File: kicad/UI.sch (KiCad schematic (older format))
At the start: 14 parts, among them SW2 SW_Push, U13 PCA9632, U14 LMV321

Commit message: 回路を改良
受光部をフォトトランジスタに変更
測距センサをVL6180Xに変更
動作電圧を3Vに変更
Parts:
- C21: renamed from C33; value 1u -> 10u
- SW2: footprint mouse:SW_PUSH -> mouse:SKRPACE010
- renumbered C32 to C20, D13 to D10, D10 to D7, D11 to D8, D12 to D9, R28 to R15, R29 to R16, R30 to R17, R31 to R18, U14 to U10, U13 to U9
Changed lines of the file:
@@
 LIBS:ftdi
 LIBS:gennum
-LIBS:graphic
 LIBS:hc11
 LIBS:ir
 LIBS:Lattice
 LIBS:leds
-LIBS:logo
 LIBS:maxim
 LIBS:mechanical
@@
 LIBS:zetex
 LIBS:Zilog
+LIBS:graphic_symbols
+LIBS:infineon
+LIBS:intersil
+LIBS:LEM
+LIBS:logic_programmable
+LIBS:RFSolutions
 LIBS:KERISE-cache
 EELAYER 25 0
@@
 $EndDescr
 $Comp
-L GND #PWR082
+L GND #PWR076
 U 1 1 57CEA2EF
 P 3700 6200
-F 0 "#PWR082" H 3700 5950 50  0001 C CNN
+F 0 "#PWR076" H 3700 5950 50  0001 C CNN
 F 1 "GND" H 3700 6050 50  0000 C CNN
 F 2 "" H 3700 6200 50  0000 C CNN
@@
 F 0 "SW2" H 3750 5900 50  0000 L CNN
 F 1 "SW_Push" H 3700 5740 50  0000 C CNN
-F 2 "mouse:SW_PUSH" H 3700 6000 50  0001 C CNN
+F 2 "mouse:SKRPACE010" H 3700 6000 50  0001 C CNN
 F 3 "" H 3700 6000 50  0001 C CNN
 	1    3700 5800
@@
 $EndComp
 $Comp
-L LMV321 U14
+L LMV321 U10
 U 1 1 5A1C2ABB
 P 5100 5800
-F 0 "U14" H 5100 6000 50  0000 L CNN
+F 0 "U10" H 5100 6000 50  0000 L CNN
 F 1 "LMV321" H 5100 5600 50  0000 L CNN
 F 2 "TO_SOT_Packages_SMD:SOT-353_SC-70-5" H 5100 5800 50  0001 L CNN
@@
 $EndComp
 $Comp
-L GND #PWR083
+L GND #PWR077
 U 1 1 5A1C53C4
 P 5800 6200
-F 0 "#PWR083" H 5800 5950 50  0001 C CNN
+F 0 "#PWR077" H 5800 5950 50  0001 C CNN
 F 1 "GND" H 5800 6050 50  0000 C CNN
 F 2 "" H 5800 6200 50  0000 C CNN
@@
 	5800 5900 5900 5900
 $Comp
-L C_Small C33
+L C_Small C21
 U 1 1 5A1C5465
 P 5700 5800
-F 0 "C33" H 5710 5870 50  0000 L CNN
-F 1 "1u" H 5710 5720 50  0000 L CNN
+F 0 "C21" H 5710 5870 50  0000 L CNN
+F 1 "10u" H 5710 5720 50  0000 L CNN
 F 2 "Capacitors_SMD:C_0402" H 5700 5800 50  0001 C CNN
 F 3 "" H 5700 5800 50  0001 C CNN
@@
 Connection ~ 5500 5800
 $Comp
-L +3.3V #PWR084
+L +3.3V #PWR078
 U 1 1 5A1C5659
 P 5000 5300
-F 0 "#PWR084" H 5000 5150 50  0001 C CNN
+F 0 "#PWR078" H 5000 5150 50  0001 C CNN
 F 1 "+3.3V" H 5000 5440 50  0000 C CNN
 F 2 "" H 5000 5300 50  0001 C CNN
@@
 	5000 5300 5000 5500
 $Comp
-L GND #PWR085
+L GND #PWR079
 U 1 1 5A1C56CE
 P 5000 6200
-F 0 "#PWR085" H 5000 5950 50  0001 C CNN
+F 0 "#PWR079" H 5000 5950 50  0001 C CNN
 F 1 "GND" H 5000 6050 50  0000 C CNN
 F 2 "" H 5000 6200 50  0000 C CNN
@@
 SDA
 $Comp
-L +3.3V #PWR086
+L +3.3V #PWR080
 U 1 1 5A202D5A
 P 4050 3150
-F 0 "#PWR086" H 4050 3000 50  0001 C CNN
+F 0 "#PWR080" H 4050 3000 50  0001 C CNN
 F 1 "+3.3V" H 4050 3290 50  0000 C CNN
 F 2 "" H 4050 3150 50  0001 C CNN
@@
 	4050 3150 4050 3650
 $Comp
-L GND #PWR087
+L GND #PWR081
 U 1 1 5A202F53
 P 4050 4650
-F 0 "#PWR087" H 4050 4400 50  0001 C CNN
+F 0 "#PWR081" H 4050 4400 50  0001 C CNN
 F 1 "GND" H 4050 4500 50  0000 C CNN
 F 2 "" H 4050 4650 50  0000 C CNN
@@
 	5050 3450 5050 3550
 $Comp
-L +3.3V #PWR088
+L +3.3V #PWR082
 U 1 1 5A204571
 P 5050 3150
-F 0 "#PWR088" H 5050 3000 50  0001 C CNN
+F 0 "#PWR082" H 5050 3000 50  0001 C CNN
 F 1 "+3.3V" H 5050 3290 50  0000 C CNN
 F 2 "" H 5050 3150 50  0001 C CNN
@@
 $EndComp
 $Comp
-L R R29
+L R R16
 U 1 1 5A20456B
 P 5050 3700
-F 0 "R29" V 5130 3700 50  0000 C CNN
+F 0 "R16" V 5130 3700 50  0000 C CNN
 F 1 "100" V 5050 3700 50  0000 C CNN
 F 2 "Resistors_SMD:R_0201" V 4980 3700 50  0001 C CNN
@@
 $EndComp
 $Comp
-L LED_Small D11
+L LED_Small D8
 U 1 1 5A204565
 P 5050 3350
-F 0 "D11" H 5000 3475 50  0000 L CNN
+F 0 "D8" H 5000 3475 50  0000 L CNN
 F 1 "LED" H 5000 3250 50  0000 L CNN
 F 2 "LEDs:LED_0402" V 5050 3350 50  0001 C CNN
@@
 	4750 3450 4750 3550
 $Comp
-L +3.3V #PWR089
+L +3.3V #PWR083
 U 1 1 5A203D72
 P 4750 3150
-F 0 "#PWR089" H 4750 3000 50  0001 C CNN
+F 0 "#PWR083" H 4750 3000 50  0001 C CNN
 F 1 "+3.3V" H 4750 3290 50  0000 C CNN
 F 2 "" H 4750 3150 50  0001 C CNN
@@
 $EndComp
 $Comp
-L R R28
+L R R15
 U 1 1 5A1FD2AD
 P 4750 3700
-F 0 "R28" V 4830 3700 50  0000 C CNN
+F 0 "R15" V 4830 3700 50  0000 C CNN
 F 1 "100" V 4750 3700 50  0000 C CNN
 F 2 "Resistors_SMD:R_0201" V 4680 3700 50  0001 C CNN
@@
 $EndComp
 $Comp
-L LED_Small D10
+L LED_Small D7
 U 1 1 5A203147
 P 4750 3350
-F 0 "D10" H 4700 3475 50  0000 L CNN
+F 0 "D7" H 4700 3475 50  0000 L CNN
 F 1 "LED" H 4700 3250 50  0000 L CNN
 F 2 "LEDs:LED_0402" V 4750 3350 50  0001 C CNN
@@
 	5650 3450 5650 3550
 $Comp
-L +3.3V #PWR090
+L +3.3V #PWR084
 U 1 1 5A20460C
 P 5650 3150
-F 0 "#PWR090" H 5650 3000 50  0001 C CNN
+F 0 "#PWR084" H 5650 3000 50  0001 C CNN
 F 1 "+3.3V" H 5650 3290 50  0000 C CNN
 F 2 "" H 5650 3150 50  0001 C CNN
@@
 $EndComp
 $Comp
-L R R31
+L R R18
 U 1 1 5A204612
 P 5650 3700
-F 0 "R31" V 5730 3700 50  0000 C CNN
+F 0 "R18" V 5730 3700 50  0000 C CNN
 F 1 "100" V 5650 3700 50  0000 C CNN
 F 2 "Resistors_SMD:R_0201" V 5580 3700 50  0001 C CNN
@@
 $EndComp
 $Comp
-L LED_Small D13
+L LED_Small D10
 U 1 1 5A204618
 P 5650 3350
-F 0 "D13" H 5600 3475 50  0000 L CNN
+F 0 "D10" H 5600 3475 50  0000 L CNN
 F 1 "LED" H 5600 3250 50  0000 L CNN
 F 2 "LEDs:LED_0402" V 5650 3350 50  0001 C CNN
@@
 	5350 3450 5350 3550
 $Comp
-L +3.3V #PWR091
+L +3.3V #PWR085
 U 1 1 5A204620
 P 5350 3150
-F 0 "#PWR091" H 5350 3000 50  0001 C CNN
+F 0 "#PWR085" H 5350 3000 50  0001 C CNN
 F 1 "+3.3V" H 5350 3290 50  0000 C CNN
 F 2 "" H 5350 3150 50  0001 C CNN
@@
 $EndComp
 $Comp
-L R R30
+L R R17
 U 1 1 5A204626
 P 5350 3700
-F 0 "R30" V 5430 3700 50  0000 C CNN
+F 0 "R17" V 5430 3700 50  0000 C CNN
 F 1 "100" V 5350 3700 50  0000 C CNN
 F 2 "Resistors_SMD:R_0201" V 5280 3700 50  0001 C CNN
@@
 $EndComp
 $Comp
-L LED_Small D12
+L LED_Small D9
 U 1 1 5A20462C
 P 5350 3350
-F 0 "D12" H 5300 3475 50  0000 L CNN
+F 0 "D9" H 5300 3475 50  0000 L CNN
 F 1 "LED" H 5300 3250 50  0000 L CNN
 F 2 "LEDs:LED_0402" V 5350 3350 50  0001 C CNN
@@
 	5650 4250 5650 3850
 $Comp
-L C_Small C32
+L C_Small C20
 U 1 1 5A2A1F42
 P 3850 3450
-F 0 "C32" H 3860 3520 50  0000 L CNN
+F 0 "C20" H 3860 3520 50  0000 L CNN
 F 1 "0.1u" H 3860 3370 50  0000 L CNN
 F 2 "Capacitors_SMD:C_0201" H 3850 3450 50  0001 C CNN
@@
 $EndComp
 $Comp
-L GND #PWR092
+L GND #PWR086
 U 1 1 5A2A2041
 P 3850 3550
-F 0 "#PWR092" H 3850 3300 50  0001 C CNN
+F 0 "#PWR086" H 3850 3300 50  0001 C CNN
 F 1 "GND" H 3850 3400 50  0000 C CNN
 F 2 "" H 3850 3550 50  0001 C CNN
@@
 Connection ~ 4050 3250
 $Comp
-L PCA9632 U13
+L PCA9632 U9
 U 1 1 5A2BFCCE
 P 4050 4100
-F 0 "U13" H 3550 4425 50  0000 L CNN
+F 0 "U9" H 3550 4425 50  0000 L CNN
 F 1 "PCA9632" H 4100 4425 50  0000 L CNN
 F 2 "mouse:DFN-8-1EP_3x3mm_Pitch0.5mm" H 4100 3800 50  0001 L CNN

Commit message: 部品を配置
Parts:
- removed C21: 10u, Capacitors_SMD:C_0402, symbol C_Small
- removed U10: LMV321, TO_SOT_Packages_SMD:SOT-353_SC-70-5, symbol LMV321
- added C19: 0.1u, Capacitors_SMD:C_0201_NoSilk, symbol C_Small
- C18: renamed from C20; footprint Capacitors_SMD:C_0201 -> Capacitors_SMD:C_0201_NoSilk
- R17: renamed from R15; footprint Resistors_SMD:R_0201 -> Resistors_SMD:R_0201_NoSilk
- R18: renamed from R16; footprint Resistors_SMD:R_0201 -> Resistors_SMD:R_0201_NoSilk
- R19: renamed from R17; footprint Resistors_SMD:R_0201 -> Resistors_SMD:R_0201_NoSilk
- R20: renamed from R18; footprint Resistors_SMD:R_0201 -> Resistors_SMD:R_0201_NoSilk
- SW2: footprint mouse:SKRPACE010 -> mouse:EVPBB
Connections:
- wire segments 33 -> 27
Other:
- moved on the sheet: LS1, SW2
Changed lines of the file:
@@
 $Descr A4 11693 8268
 encoding utf-8
-Sheet 15 15
+Sheet 15 16
 Title ""
 Date ""
@@
 $EndDescr
 $Comp
-L GND #PWR076
+L GND #PWR074
 U 1 1 57CEA2EF
-P 3700 6200
-F 0 "#PWR076" H 3700 5950 50  0001 C CNN
-F 1 "GND" H 3700 6050 50  0000 C CNN
-F 2 "" H 3700 6200 50  0000 C CNN
-F 3 "" H 3700 6200 50  0000 C CNN
-	1    3700 6200
-	1    0    0    -1
-$EndComp
-Text HLabel 3700 5300 0    60   Input ~ 0
+P 6500 4600
+F 0 "#PWR074" H 6500 4350 50  0001 C CNN
+F 1 "GND" H 6500 4450 50  0000 C CNN
+F 2 "" H 6500 4600 50  0000 C CNN
+F 3 "" H 6500 4600 50  0000 C CNN
+	1    6500 4600
+	1    0    0    -1
+$EndComp
+Text HLabel 6500 3700 0    60   Input ~ 0
 BUTTON
 Text Notes 3300 2700 0    100  ~ 0
@@
 L Speaker LS1
 U 1 1 594AA6DF
-P 6100 5800
-F 0 "LS1" H 6150 6025 50  0000 R CNN
-F 1 "Speaker" H 6150 5950 50  0000 R CNN
-F 2 "mouse:SMT-0440-S-R" H 6100 5600 50  0001 C CNN
-F 3 "" H 6090 5750 50  0001 C CNN
-	1    6100 5800
-	1    0    0    -1
-$EndComp
-Wire Wire Line
-	3700 5300 3700 5600
-Wire Wire Line
-	3700 6200 3700 6000
+P 7500 4300
+F 0 "LS1" H 7550 4525 50  0000 R CNN
+F 1 "Speaker" H 7550 4450 50  0000 R CNN
+F 2 "mouse:SMT-0440-S-R" H 7500 4100 50  0001 C CNN
+F 3 "" H 7490 4250 50  0001 C CNN
+	1    7500 4300
+	1    0    0    -1
+$EndComp
+Wire Wire Line
+	6500 3700 6500 4000
+Wire Wire Line
+	6500 4600 6500 4400
 $Comp
 L SW_Push SW2
 U 1 1 594AAC95
-P 3700 5800
-F 0 "SW2" H 3750 5900 50  0000 L CNN
-F 1 "SW_Push" H 3700 5740 50  0000 C CNN
-F 2 "mouse:SKRPACE010" H 3700 6000 50  0001 C CNN
-F 3 "" H 3700 6000 50  0001 C CNN
-	1    3700 5800
+P 6500 4200
+F 0 "SW2" H 6550 4300 50  0000 L CNN
+F 1 "SW_Push" H 6500 4140 50  0000 C CNN
+F 2 "mouse:EVPBB" H 6500 4400 50  0001 C CNN
+F 3 "" H 6500 4400 50  0001 C CNN
+	1    6500 4200
 	0    1    1    0
 $EndComp
 $Comp
-L LMV321 U10
-U 1 1 5A1C2ABB
-P 5100 5800
-F 0 "U10" H 5100 6000 50  0000 L CNN
-F 1 "LMV321" H 5100 5600 50  0000 L CNN
-F 2 "TO_SOT_Packages_SMD:SOT-353_SC-70-5" H 5100 5800 50  0001 L CNN
-F 3 "" H 5100 5800 50  0001 C CNN
-	1    5100 5800
-	1    0    0    -1
-$EndComp
-$Comp
-L GND #PWR077
+L GND #PWR075
 U 1 1 5A1C53C4
-P 5800 6200
-F 0 "#PWR077" H 5800 5950 50  0001 C CNN
-F 1 "GND" H 5800 6050 50  0000 C CNN
-F 2 "" H 5800 6200 50  0000 C CNN
-F 3 "" H 5800 6200 50  0000 C CNN
-	1    5800 6200
-	1    0    0    -1
-$EndComp
-Wire Wire Line
-	5800 6200 5800 5900
-Wire Wire Line
-	5800 5900 5900 5900
-$Comp
-L C_Small C21
-U 1 1 5A1C5465
-P 5700 5800
-F 0 "C21" H 5710 5870 50  0000 L CNN
-F 1 "10u" H 5710 5720 50  0000 L CNN
-F 2 "Capacitors_SMD:C_0402" H 5700 5800 50  0001 C CNN
-F 3 "" H 5700 5800 50  0001 C CNN
-	1    5700 5800
-	0    1    1    0
-$EndComp
-Wire Wire Line
-	5900 5800 5800 5800
-Wire Wire Line
-	5400 5800 5600 5800
-Wire Wire Line
-	5500 5800 5500 5400
-Wire Wire Line
-	5500 5400 4700 5400
-Wire Wire Line
-	4700 5400 4700 5900
-Wire Wire Line
-	4700 5900 4800 5900
-Connection ~ 5500 5800
-$Comp
-L +3.3V #PWR078
-U 1 1 5A1C5659
-P 5000 5300
-F 0 "#PWR078" H 5000 5150 50  0001 C CNN
-F 1 "+3.3V" H 5000 5440 50  0000 C CNN
-F 2 "" H 5000 5300 50  0001 C CNN
-F 3 "" H 5000 5300 50  0001 C CNN
-	1    5000 5300
-	1    0    0    -1
-$EndComp
-Wire Wire Line
-	5000 5300 5000 5500
-$Comp
-L GND #PWR079
-U 1 1 5A1C56CE
-P 5000 6200
-F 0 "#PWR079" H 5000 5950 50  0001 C CNN
-F 1 "GND" H 5000 6050 50  0000 C CNN
-F 2 "" H 5000 6200 50  0000 C CNN
-F 3 "" H 5000 6200 50  0000 C CNN
-	1    5000 6200
-	1    0    0    -1
-$EndComp
-Wire Wire Line
-	5000 6200 5000 6100
-Text HLabel 4600 5700 0    60   Input ~ 0
+P 7200 4600
+F 0 "#PWR075" H 7200 4350 50  0001 C CNN
+F 1 "GND" H 7200 4450 50  0000 C CNN
+F 2 "" H 7200 4600 50  0000 C CNN
+F 3 "" H 7200 4600 50  0000 C CNN
+	1    7200 4600
+	1    0    0    -1
+$EndComp
+Wire Wire Line
+	7200 4400 7300 4400
+Wire Wire Line
+	7200 4300 7300 4300
+Text HLabel 7200 3700 0    60   Input ~ 0
 SPEAKER
-Wire Wire Line
-	4600 5700 4800 5700
 Text HLabel 3450 3950 0    60   Input ~ 0
 SCL
@@
 SDA
 $Comp
-L +3.3V #PWR080
+L +3.3V #PWR076
 U 1 1 5A202D5A
 P 4050 3150
-F 0 "#PWR080" H 4050 3000 50  0001 C CNN
+F 0 "#PWR076" H 4050 3000 50  0001 C CNN
 F 1 "+3.3V" H 4050 3290 50  0000 C CNN
 F 2 "" H 4050 3150 50  0001 C CNN
@@
 	4050 3150 4050 3650
 $Comp
-L GND #PWR081
+L GND #PWR077
 U 1 1 5A202F53
 P 4050 4650
-F 0 "#PWR081" H 4050 4400 50  0001 C CNN
+F 0 "#PWR077" H 4050 4400 50  0001 C CNN
 F 1 "GND" H 4050 4500 50  0000 C CNN
 F 2 "" H 4050 4650 50  0000 C CNN
@@
 	5050 3450 5050 3550
 $Comp
-L +3.3V #PWR082
+L +3.3V #PWR078
 U 1 1 5A204571
 P 5050 3150
-F 0 "#PWR082" H 5050 3000 50  0001 C CNN
+F 0 "#PWR078" H 5050 3000 50  0001 C CNN
 F 1 "+3.3V" H 5050 3290 50  0000 C CNN
 F 2 "" H 5050 3150 50  0001 C CNN
@@
 $EndComp
 $Comp
-L R R16
+L R R18
 U 1 1 5A20456B
 P 5050 3700
-F 0 "R16" V 5130 3700 50  0000 C CNN
+F 0 "R18" V 5130 3700 50  0000 C CNN
 F 1 "100" V 5050 3700 50  0000 C CNN
-F 2 "Resistors_SMD:R_0201" V 4980 3700 50  0001 C CNN
+F 2 "Resistors_SMD:R_0201_NoSilk" V 4980 3700 50  0001 C CNN
 F 3 "" H 5050 3700 50  0001 C CNN
 	1    5050 3700
@@
 	4750 3450 4750 3550
 $Comp
-L +3.3V #PWR083
+L +3.3V #PWR079
 U 1 1 5A203D72
 P 4750 3150
-F 0 "#PWR083" H 4750 3000 50  0001 C CNN
+F 0 "#PWR079" H 4750 3000 50  0001 C CNN
 F 1 "+3.3V" H 4750 3290 50  0000 C CNN
 F 2 "" H 4750 3150 50  0001 C CNN
@@
 $EndComp
 $Comp
-L R R15
+L R R17
 U 1 1 5A1FD2AD
 P 4750 3700
-F 0 "R15" V 4830 3700 50  0000 C CNN
+F 0 "R17" V 4830 3700 50  0000 C CNN
 F 1 "100" V 4750 3700 50  0000 C CNN
-F 2 "Resistors_SMD:R_0201" V 4680 3700 50  0001 C CNN
+F 2 "Resistors_SMD:R_0201_NoSilk" V 4680 3700 50  0001 C CNN
 F 3 "" H 4750 3700 50  0001 C CNN
 	1    4750 3700
@@
 	5650 3450 5650 3550
 $Comp
-L +3.3V #PWR084
+L +3.3V #PWR080
 U 1 1 5A20460C
 P 5650 3150
-F 0 "#PWR084" H 5650 3000 50  0001 C CNN
+F 0 "#PWR080" H 5650 3000 50  0001 C CNN
 F 1 "+3.3V" H 5650 3290 50  0000 C CNN
 F 2 "" H 5650 3150 50  0001 C CNN
@@
 $EndComp
 $Comp
-L R R18
+L R R20
 U 1 1 5A204612
 P 5650 3700
-F 0 "R18" V 5730 3700 50  0000 C CNN
+F 0 "R20" V 5730 3700 50  0000 C CNN
 F 1 "100" V 5650 3700 50  0000 C CNN
-F 2 "Resistors_SMD:R_0201" V 5580 3700 50  0001 C CNN
+F 2 "Resistors_SMD:R_0201_NoSilk" V 5580 3700 50  0001 C CNN
 F 3 "" H 5650 3700 50  0001 C CNN
 	1    5650 3700
@@
 	5350 3450 5350 3550
 $Comp
-L +3.3V #PWR085
+L +3.3V #PWR081
 U 1 1 5A204620
 P 5350 3150
-F 0 "#PWR085" H 5350 3000 50  0001 C CNN
+F 0 "#PWR081" H 5350 3000 50  0001 C CNN
 F 1 "+3.3V" H 5350 3290 50  0000 C CNN
 F 2 "" H 5350 3150 50  0001 C CNN
@@
 $EndComp
 $Comp
-L R R17
+L R R19
 U 1 1 5A204626
 P 5350 3700
-F 0 "R17" V 5430 3700 50  0000 C CNN
+F 0 "R19" V 5430 3700 50  0000 C CNN
 F 1 "100" V 5350 3700 50  0000 C CNN
-F 2 "Resistors_SMD:R_0201" V 5280 3700 50  0001 C CNN
+F 2 "Resistors_SMD:R_0201_NoSilk" V 5280 3700 50  0001 C CNN
 F 3 "" H 5350 3700 50  0001 C CNN
 	1    5350 3700
@@
 	5650 4250 5650 3850
 $Comp
-L C_Small C20
+L C_Small C18
 U 1 1 5A2A1F42
 P 3850 3450
-F 0 "C20" H 3860 3520 50  0000 L CNN
+F 0 "C18" H 3860 3520 50  0000 L CNN
 F 1 "0.1u" H 3860 3370 50  0000 L CNN
-F 2 "Capacitors_SMD:C_0201" H 3850 3450 50  0001 C CNN
+F 2 "Capacitors_SMD:C_0201_NoSilk" H 3850 3450 50  0001 C CNN
 F 3 "" H 3850 3450 50  0001 C CNN
 	1    3850 3450
@@
 $EndComp
 $Comp
-L GND #PWR086
+L GND #PWR082
 U 1 1 5A2A2041
 P 3850 3550
-F 0 "#PWR086" H 3850 3300 50  0001 C CNN
+F 0 "#PWR082" H 3850 3300 50  0001 C CNN
 F 1 "GND" H 3850 3400 50  0000 C CNN
 F 2 "" H 3850 3550 50  0001 C CNN
@@
 	1    0    0    -1
 $EndComp
+Wire Wire Line
+	7200 3800 7200 3700
+Wire Wire Line
+	7200 4000 7200 4300
+Wire Wire Line
+	7200 4400 7200 4600
+$Comp
+L C_Small C19
+U 1 1 5AB1BA0C
+P 7200 3900
+F 0 "C19" H 7210 3970 50  0000 L CNN
+F 1 "0.1u" H 7210 3820 50  0000 L CNN
+F 2 "Capacitors_SMD:C_0201_NoSilk" H 7200 3900 50  0001 C CNN
+F 3 "" H 7200 3900 50  0001 C CNN
+	1    7200 3900
+	1    0    0    -1
+$EndComp

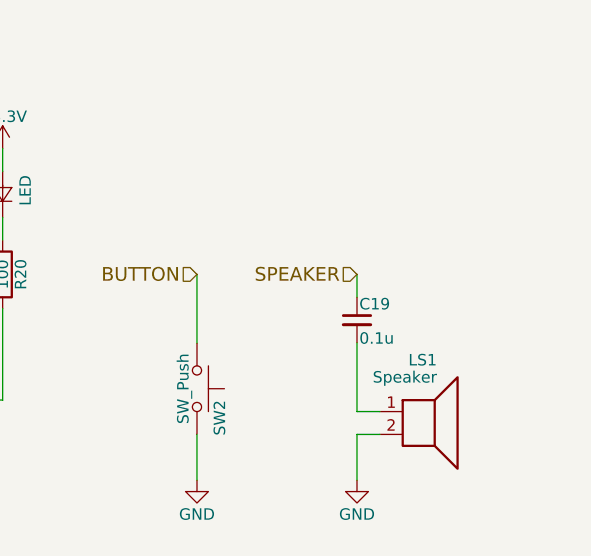
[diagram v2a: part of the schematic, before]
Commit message: 回路を編集 ToFを除去
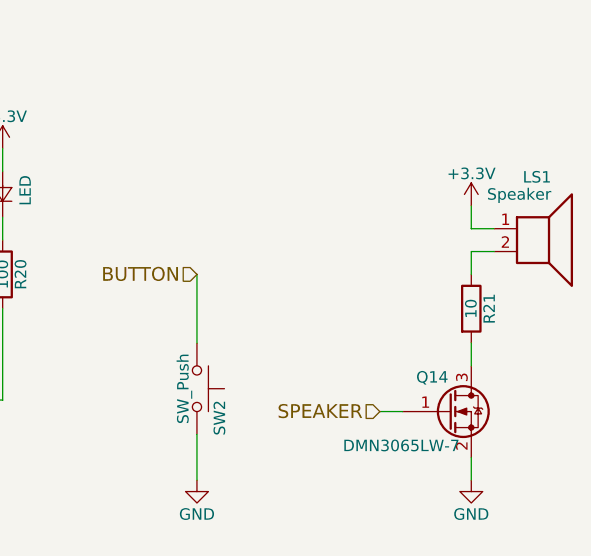
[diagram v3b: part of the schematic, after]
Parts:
- removed C19: 0.1u, Capacitors_SMD:C_0201_NoSilk, symbol C_Small
- added Q14: DMN3065LW-7, TO_SOT_Packages_SMD:SOT-323_SC-70, symbol Q_NMOS_GSD
- added R21: 10, Resistors_SMD:R_0201_NoSilk, symbol R
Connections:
- net +3V3: now also LS1.1
- net GND: now also Q14.2 (S); no longer LS1.2
- net SPEAKER: now also Q14.1 (G)
- new net: LS1.2, R21.1
- new net: Q14.3 (D), R21.2
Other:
- moved on the sheet: LS1
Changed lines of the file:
@@
 $Descr A4 11693 8268
 encoding utf-8
-Sheet 15 16
+Sheet 15 15
 Title ""
 Date ""
@@
 L Speaker LS1
 U 1 1 594AA6DF
-P 7500 4300
-F 0 "LS1" H 7550 4525 50  0000 R CNN
-F 1 "Speaker" H 7550 4450 50  0000 R CNN
-F 2 "mouse:SMT-0440-S-R" H 7500 4100 50  0001 C CNN
-F 3 "" H 7490 4250 50  0001 C CNN
-	1    7500 4300
+P 8000 3500
+F 0 "LS1" H 8050 3725 50  0000 R CNN
+F 1 "Speaker" H 8050 3650 50  0000 R CNN
+F 2 "mouse:SMT-0440-S-R" H 8000 3300 50  0001 C CNN
+F 3 "" H 7990 3450 50  0001 C CNN
+	1    8000 3500
 	1    0    0    -1
 $EndComp
@@
 L GND #PWR075
 U 1 1 5A1C53C4
-P 7200 4600
-F 0 "#PWR075" H 7200 4350 50  0001 C CNN
-F 1 "GND" H 7200 4450 50  0000 C CNN
-F 2 "" H 7200 4600 50  0000 C CNN
-F 3 "" H 7200 4600 50  0000 C CNN
-	1    7200 4600
-	1    0    0    -1
-$EndComp
-Wire Wire Line
-	7200 4400 7300 4400
-Wire Wire Line
-	7200 4300 7300 4300
-Text HLabel 7200 3700 0    60   Input ~ 0
+P 7700 4600
+F 0 "#PWR075" H 7700 4350 50  0001 C CNN
+F 1 "GND" H 7700 4450 50  0000 C CNN
+F 2 "" H 7700 4600 50  0000 C CNN
+F 3 "" H 7700 4600 50  0000 C CNN
+	1    7700 4600
+	1    0    0    -1
+$EndComp
+Wire Wire Line
+	7700 3600 7800 3600
+Wire Wire Line
+	7700 3500 7800 3500
+Text HLabel 7300 4300 0    60   Input ~ 0
 SPEAKER
 Text HLabel 3450 3950 0    60   Input ~ 0
@@
 	1    0    0    -1
 $EndComp
-Wire Wire Line
-	7200 3800 7200 3700
-Wire Wire Line
-	7200 4000 7200 4300
-Wire Wire Line
-	7200 4400 7200 4600
-$Comp
-L C_Small C19
-U 1 1 5AB1BA0C
-P 7200 3900
-F 0 "C19" H 7210 3970 50  0000 L CNN
-F 1 "0.1u" H 7210 3820 50  0000 L CNN
-F 2 "Capacitors_SMD:C_0201_NoSilk" H 7200 3900 50  0001 C CNN
-F 3 "" H 7200 3900 50  0001 C CNN
-	1    7200 3900
-	1    0    0    -1
-$EndComp
+$Comp
+L Q_NMOS_GSD Q14
+U 1 1 5B6723D7
+P 7600 4300
+F 0 "Q14" H 7600 4450 50  0000 R CNN
+F 1 "DMN3065LW-7" H 7650 4150 50  0000 R CNN
+F 2 "TO_SOT_Packages_SMD:SOT-323_SC-70" H 7800 4400 50  0001 C CNN
+F 3 "" H 7600 4300 50  0000 C CNN
+	1    7600 4300
+	1    0    0    -1
+$EndComp
+Wire Wire Line
+	7300 4300 7400 4300
+$Comp
+L +3.3V #PWR083
+U 1 1 5B6724D4
+P 7700 3400
+F 0 "#PWR083" H 7700 3250 50  0001 C CNN
+F 1 "+3.3V" H 7700 3540 50  0000 C CNN
+F 2 "" H 7700 3400 50  0001 C CNN
+F 3 "" H 7700 3400 50  0001 C CNN
+	1    7700 3400
+	1    0    0    -1
+$EndComp
+$Comp
+L R R21
+U 1 1 5B6725CD
+P 7700 3850
+F 0 "R21" V 7780 3850 50  0000 C CNN
+F 1 "10" V 7700 3850 50  0000 C CNN
+F 2 "Resistors_SMD:R_0201_NoSilk" V 7630 3850 50  0001 C CNN
+F 3 "" H 7700 3850 50  0001 C CNN
+	1    7700 3850
+	1    0    0    -1
+$EndComp
+Wire Wire Line
+	7700 3500 7700 3400
+Wire Wire Line
+	7700 3600 7700 3700
+Wire Wire Line
+	7700 4500 7700 4600
+Wire Wire Line
+	7700 4000 7700 4100
 $EndSCHEMATC

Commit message: 部品を配置 kicad5
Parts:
- removed SW2: SW_Push, mouse:EVPBB, symbol SW_Push
- added SW2: UPLOAD, mouse:EVPBB, symbol Switch:SW_Push
- C16: renamed from C18; symbol C_Small -> Device:C_Small
- D10, D7, D8, D9: symbol LED_Small -> Device:LED_Small
- LS1: symbol Speaker -> Device:Speaker
- Q14: symbol Q_NMOS_GSD -> Device:Q_NMOS_GSD
- R15: renamed from R17; symbol R -> Device:R
- R16: renamed from R18; symbol R -> Device:R
- R17: renamed from R19; symbol R -> Device:R
- R18: renamed from R20; symbol R -> Device:R
- R19: renamed from R21; symbol R -> Device:R
- U8: renamed from U9; symbol PCA9632 -> KERISE:PCA9632
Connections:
- net BUTTON: now also SW2.1
- net GND: now also SW2.2
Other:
- moved on the sheet: LS1, Q14, R19
